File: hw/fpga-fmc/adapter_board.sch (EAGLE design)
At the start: 19 parts, among them J1 5569262-1, J2 ASP-134488-01, U1 LTM2881, U10 LTM2881, U11 LTM2881, U12 LTM2881, U13 LTM2881, U14 LTM2881, U15 LTM2881, U16 LTM2881, U2 LTM2881, U3 LTM2881, U4 LTM2881, U5 LTM2881, U6 LTM2881, U7 LTM2881, U8 LTM2881, U9 LTM2881

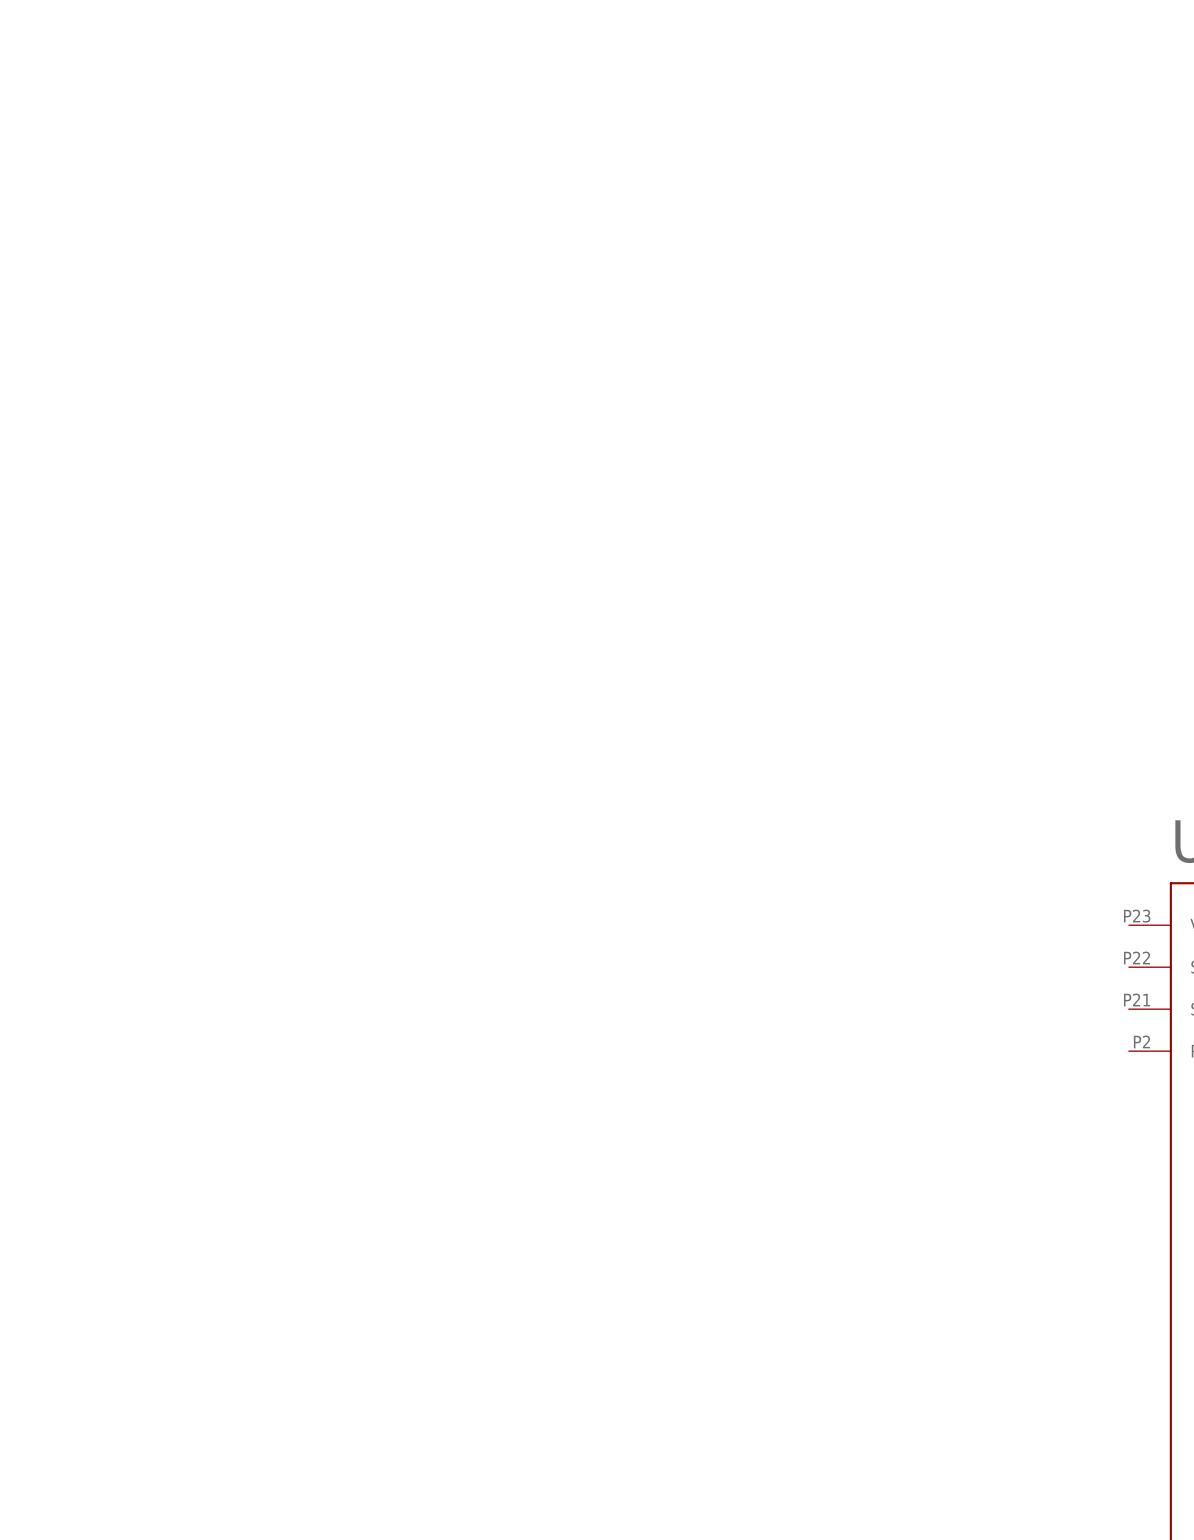
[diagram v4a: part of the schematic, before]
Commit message: fpga-fmc: add 4 channel isolator ic
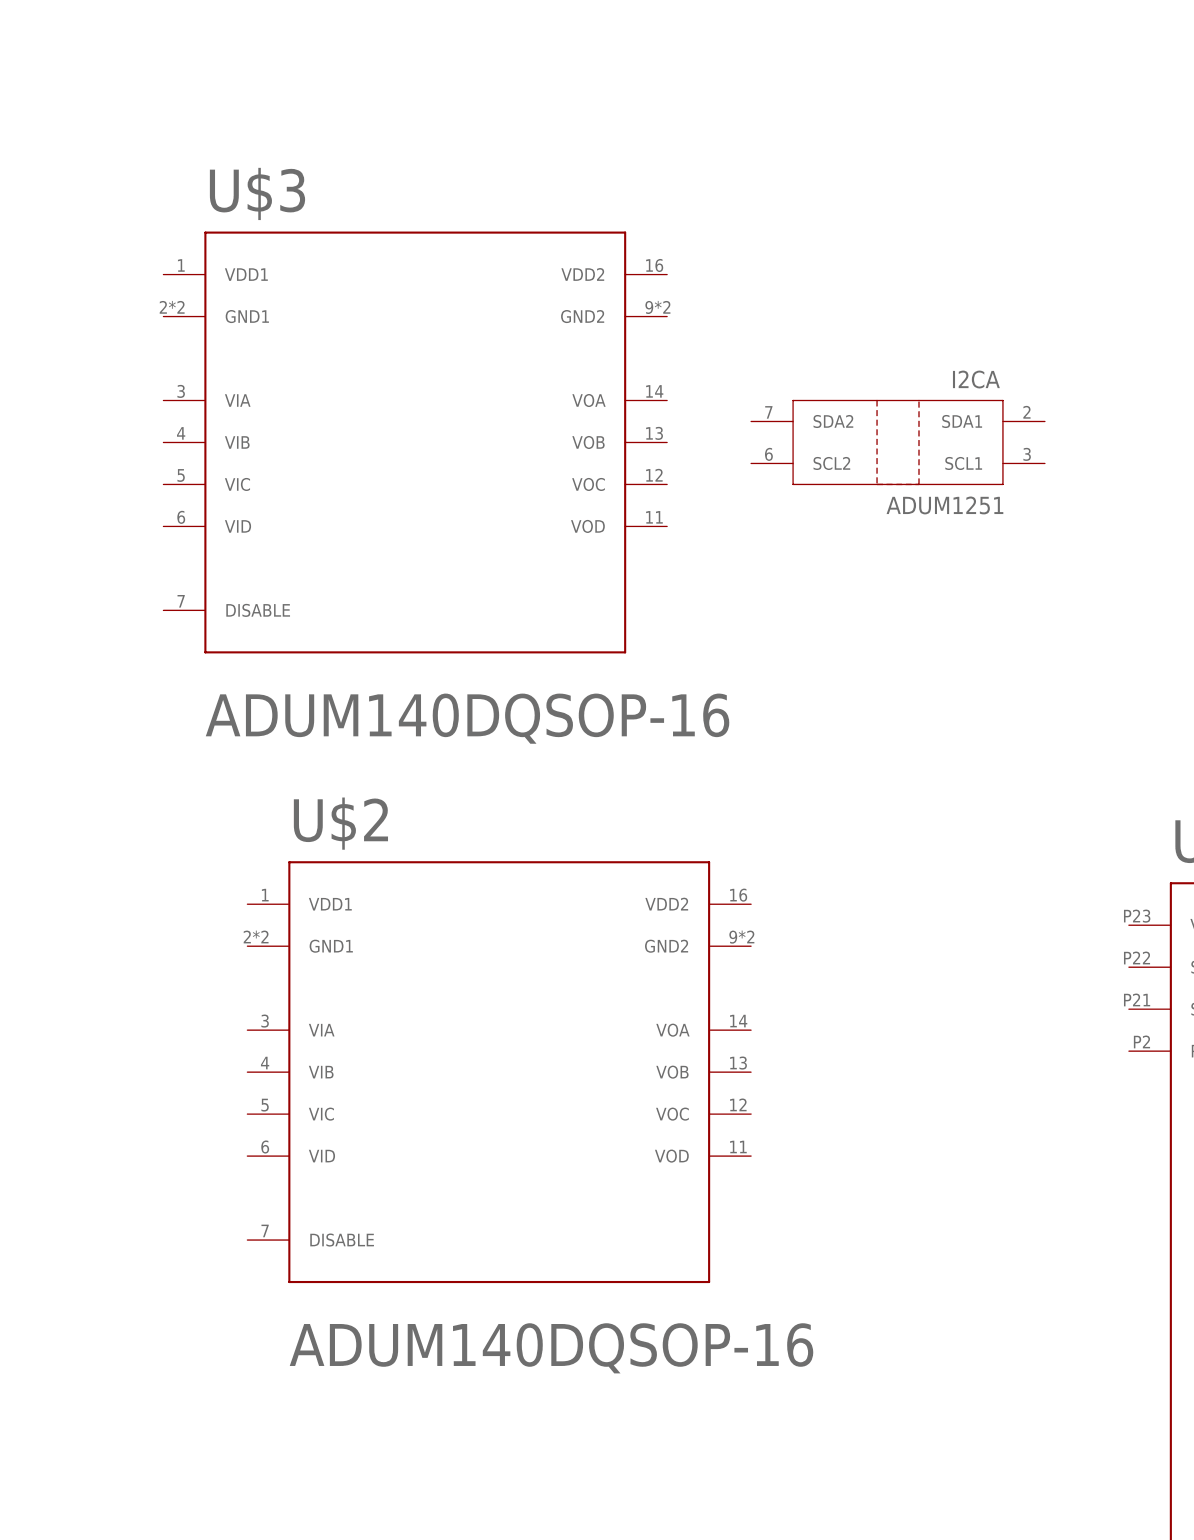
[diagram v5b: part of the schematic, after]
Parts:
- added I2C: ADUM1251, ADUM1251WARZ:ADUM1251WARZ
- added U$2, U$3: ADUM140DQSOP-16, parts:ADUM140DQSOP-16
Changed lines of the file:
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@@
 <part name="U16" library="parts" deviceset="LTM2881" device=""/>
 <part name="U$1" library="parts" deviceset="PCA9548A" device=""/>
+<part name="I2C" library="ADUM1251WARZ" deviceset="ADUM1251WARZ" device="" value="ADUM1251">
+<attribute name="DIGIKEY" value="ADUM1251ARZ-RL7TR-ND"/>
+</part>
+<part name="U$2" library="parts" deviceset="ADUM140D" device="QSOP-16" package3d_urn="urn:adsk.eagle:package:3955/1"/>
+<part name="U$3" library="parts" deviceset="ADUM140D" device="QSOP-16" package3d_urn="urn:adsk.eagle:package:3955/1"/>
 </parts>
 <sheets>
@@
 <attribute name="NAME" x="10.16" y="-10.16" size="5.08" layer="95"/>
 <attribute name="VALUE" x="10.16" y="-129.54" size="5.08" layer="95"/>
+</instance>
+<instance part="I2C" gate="A" x="-22.86" y="40.64" smashed="yes" rot="MR0">
+<attribute name="NAME" x="-10.5156" y="47.2186" size="2.0828" layer="95" ratio="6" rot="SMR0"/>
+<attribute name="VALUE" x="-9.8806" y="31.9786" size="2.0828" layer="96" ratio="6" rot="SMR0"/>
+<attribute name="DIGIKEY" x="-22.86" y="40.64" size="1.778" layer="96" rot="MR0" display="off"/>
+</instance>
+<instance part="U$2" gate="G$1" x="-71.12" y="-35.56" smashed="yes">
+<attribute name="NAME" x="-96.52" y="-7.62" size="5.08" layer="95"/>
+<attribute name="VALUE" x="-96.52" y="-71.12" size="5.08" layer="96"/>
+</instance>
+<instance part="U$3" gate="G$1" x="-81.28" y="40.64" smashed="yes">
+<attribute name="NAME" x="-106.68" y="68.58" size="5.08" layer="95"/>
+<attribute name="VALUE" x="-106.68" y="5.08" size="5.08" layer="96"/>
 </instance>
 </instances>
@@
 will not be understood (or retained) with this version.
 </note>
+<note version="8.3" severity="warning">
+Since Version 8.3, EAGLE supports the association of 3D packages
+with devices in libraries, schematics, and board files. Those 3D
+packages will not be understood (or retained) with this version.
+</note>
 </compatibility>

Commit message: hw/fpga-fmc: add and route rs485 transceiver for 3 channels
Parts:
- removed U10, U11, U12, U13, U14, U15, U16, U7, U8, U9: LTM2881, parts:LTM2881
- added C1, C10, C11, C12, C13, C14, C2, C3, C5, C6, C7, C8, C9: 100n, rcl:C-EUC0805
- added C4: 1u, rcl:C-EUC0805
- added R1, R10, R11, R12, R13, R14, R15, R16, R17, R18, R19, R20, R21, R22, R24, R26, R28, R3, R30, R4, R5, R6, R7, R8, R9: (no value), rcl:R-EU_R0805
- added R2, R23, R25, R27, R29, R31: 100R, rcl:R-EU_R0805
- U1, U2, U3, U4, U5, U6: value LTM2881 -> ADM3066E; device parts:LTM2881 -> parts:ADM3066E
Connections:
- net N$10 renamed RJ6_SDO
- net N$11 renamed RJ6_SCL
- net N$12 renamed RJ6_DATA_P
- net N$13 renamed RJ6_CONV
- net N$15 renamed RJ6_DATA_N
- net N$16 renamed RJ6_CLK_N
- net N$17 renamed RJ6_CLK_P
- net N$2 renamed RJ5_SDO
- net N$26 renamed RJ7_SDO
- net N$27 renamed RJ7_SCL
- net N$29 renamed RJ7_CONV
- net N$3 renamed RJ5_SCL
- net N$34 renamed RJ8_SDO
- net N$35 renamed RJ8_SCL
- net N$37 renamed RJ8_CONV
- net N$4 renamed RJ5_DATA_P
- net N$5 renamed RJ5_CONV
- net N$7 renamed RJ5_DATA_N
- net N$8 renamed RJ5_CLK_N
- net N$9 renamed RJ5_CLK_P
- removed net N$28: J1.7.6
- removed net N$31: J1.7.3
- removed net N$32: J1.7.2
- removed net N$33: J1.7.1
- removed net N$36: J1.8.6
- removed net N$39: J1.8.3
- removed net N$40: J1.8.2
- removed net N$57: J1.8.1
- removed net U1_ON: U1.ON
- new net 3V3: C3.2, C4.2, U$1.VCC
- new net 5V: C10.1, C12.1, C14.1, C2.1, C6.1, C8.1, R10.2, R11.2, R12.2, R13.2, R14.2, R15.2, R16.2, R17.2, R18.2, R19.2, R20.2, R21.2, R3.2, R4.2, R8.2, R9.2, U1.VCC, U2.VCC, U3.VCC, U4.VCC, U5.VCC, U6.VCC
- new net LSIO1: R2.1, U1.DI, U1.RO
- new net LSIO2: R23.1, U2.DI, U2.RO
- new net LSIO3: R25.1, U3.DI, U3.RO
- new net LSIO4: R27.1, U4.DI, U4.RO
- new net LSIO5: R29.1, U5.DI, U5.RO
- new net LSIO6: R31.1, U6.DI, U6.RO
- new net N$1: R3.1, U$1.SD0
- new net N$14: R8.1, U$1.SD1
- new net N$21: U$1.SD3
- new net N$22: R12.1, R13.1, U$1.SC3
- new net N$24: R15.1, U$1.SC4
- new net N$46: R7.1, U$1.RESET
- new net N$6: R4.1, U$1.SC0
- new net RJ7_CLK_N: J1.7.2, R28.2, U5.B
- new net RJ7_CLK_P: J1.7.1, R28.1, U5.A
- new net RJ7_DATA_N: J1.7.3, R30.2, U6.B
- new net RJ7_DATA_P: J1.7.6, R30.1, U6.A
- new net RJ8_CLK_N: J1.8.2, R1.2, U1.B
- new net RJ8_CLK_P: J1.8.1, R1.1, U1.A
- new net RJ8_DATA_N: J1.8.3, R22.2, U2.B
- new net RJ8_DATA_P: J1.8.6, R22.1, U2.A
- net +3V3: no longer U1.VCC1
- net 0V: now also C1.2, C10.2, C11.2, C12.2, C13.2, C14.2, C2.2, C3.1, C4.1, C5.2, C6.2, C7.2, C8.2, C9.2, U$1.A0, U$1.A1, U$1.A2, U$1.GND, U1.GND, U2.GND, U3.GND, U4.GND, U5.GND, U6.GND; no longer U1.GND1
- net 1V8: now also C1.1, C11.1, C13.1, C5.1, C7.1, C9.1, R5.2, R6.2, R7.2, U1.VIO, U2.VIO, U3.VIO, U4.VIO, U5.VIO, U6.VIO; no longer U1.VL
- net FMC_DP0_C2M_N: now also U1.DE, U1.RE
- net FMC_DP0_C2M_P: now also R2.2
- net FMC_DP0_M2C_N: now also R27.2
- net FMC_DP0_M2C_P: now also U4.DE, U4.RE
- net FMC_LA00_CC_N: now also R23.2
- net FMC_LA00_CC_P: now also U2.DE, U2.RE
- net FMC_LA02_N: now also R25.2
- net FMC_LA02_P: now also U3.DE, U3.RE
- net FMC_LA03_N: now also R31.2
- net FMC_LA03_P: now also U6.DE, U6.RE
- net FMC_LA04_N: now also R29.2
- net FMC_LA04_P: now also U5.DE, U5.RE
- net FMC_LA06_N: no longer U1.DI
- net FMC_LA06_P: no longer U1.RO
- net N$18: now also R9.1, U$1.SC1; no longer U1.RE
- net N$19: now also R10.1, U$1.SD2; no longer U1.TE
- net N$20: now also R11.1, U$1.SC2; no longer U1.DE
- net N$23: now also R14.1, U$1.SD4; no longer U1.DOUT
- net N$25: now also R16.1, U$1.SD5; no longer U1.VCC2
- net N$30: now also R17.1, U$1.SC5; no longer U1.A
- net N$38: now also R18.1, U$1.SD6; no longer U1.B
- net N$41: now also R19.1, U$1.SC6; no longer U1.Y
- net N$42: now also R20.1, U$1.SD7; no longer U1.Z
- net N$43: now also R21.1, U$1.SC7; no longer U1.SLO
- net N$44: now also R5.1, U$1.SDA; no longer U1.DIN
- net N$45: now also R6.1, U$1.SCL; no longer U1.GND2
- net RJ4_CLK_N: now also R24.2, U3.B
- net RJ4_CLK_P: now also R24.1, U3.A
- net RJ4_DATA_N: now also R26.2, U4.B
- net RJ4_DATA_P: now also R26.1, U4.A
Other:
- note added: "CLK IO 4"
- note added: "CLK IO 7"
- note added: "CLK IO 8"
- note added: "DATA IO 4"
- note added: "DATA IO 7"
- note added: "DATA IO 8"
- moved on the sheet: U$1

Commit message: fpga-fmc: add i2c circuit and level shifter for conv signal
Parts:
- removed I2C: ADUM1251, ADUM1251WARZ:ADUM1251WARZ
- removed U$3: ADUM140DQSOP-16, parts:ADUM140DQSOP-16
- added C15, C16, C17, C18, C19, C20, C21, C22, C23, C24, C25, C26, C27, C28, C29, C30, C31, C32, C33, C34, C35, C36, C37, C39: 100n, rcl:C-EUC0805
- added IC1: M24C02, parts:N24C02UDTG
- added R32, R34, R36, R38, R40, R42, R44, R46, R48, R50: (no value), rcl:R-EU_R0805
- added R33, R35, R37, R39, R41, R43, R45, R47, R49, R51: 100R, rcl:R-EU_R0805
- added R52: 0R, rcl:R-EU_R0805
- added U10, U11, U12, U13, U14, U15, U16, U7, U8, U9: ADM3066E, parts:ADM3066E
- added U17: TCA9548A, parts:PCA9548A
- J2: SPICEPREFIX (none) -> X
- R10, R11, R12, R13, R14, R15, R16, R17, R18, R19, R20, R21, R3, R4, R5, R6, R8, R9: value (none) -> 1k
- R7: value (none) -> 10k
- U$1: value PCA9548A -> TXS0104E; device parts:PCA9548A -> parts:TXS0104E
- U$2: value ADUM140DQSOP-16 -> TXS0104E; device parts:ADUM140DQSOP-16 -> parts:TXS0104E
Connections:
- removed net 3V3: C3.2, C4.2, U$1.VCC
- removed net N$18: R9.1, U$1.SC1
- removed net N$19: R10.1, U$1.SD2
- removed net N$20: R11.1, U$1.SC2
- removed net N$21: U$1.SD3
- removed net N$22: R12.1, R13.1, U$1.SC3
- removed net N$23: R14.1, U$1.SD4
- removed net N$24: R15.1, U$1.SC4
- removed net N$25: R16.1, U$1.SD5
- removed net N$30: R17.1, U$1.SC5
- removed net N$38: R18.1, U$1.SD6
- removed net N$41: R19.1, U$1.SC6
- removed net N$42: R20.1, U$1.SD7
- removed net N$43: R21.1, U$1.SC7
- new net 3P3VAUX: C39.2, IC1.VCC, J2D.D32, R52.2
- new net GA0: IC1.A1, J2C.C34
- new net GA1: IC1.A0, J2D.D35
- new net LSIO10: R39.1, U10.DI, U10.RO
- new net LSIO11: R41.1, U11.DI, U11.RO
- new net LSIO12: R43.1, U12.DI, U12.RO
- new net LSIO13: R45.1, U13.DI, U13.RO
- new net LSIO14: R47.1, U14.DI, U14.RO
- new net LSIO15: R49.1, U15.DI, U15.RO
- new net LSIO16: R51.1, U16.DI, U16.RO
- new net LSIO7: R33.1, U7.DI, U7.RO
- new net LSIO8: R35.1, U8.DI, U8.RO
- new net LSIO9: R37.1, U9.DI, U9.RO
- new net N$10: U$2.B4
- new net N$11: U$2.B3
- new net N$12: U$2.B2
- new net N$13: U$2.B1
- new net N$15: U$1.B3
- new net N$16: U$1.B2
- new net N$17: U$1.B1
- new net N$2: U$2.A4
- new net N$3: U$2.A3
- new net N$4: U$2.A2
- new net N$5: U$2.A1
- new net N$7: U$1.A3
- new net N$8: U$1.A2
- new net N$9: U$1.A1
- net +12V: now also C37.2
- net +3V3: now also C36.2; no longer J2D.D32
- net 0V: now also C15.2, C16.2, C17.2, C18.2, C19.2, C20.2, C21.2, C22.2, C23.2, C24.2, C25.2, C26.2, C27.2, C28.2, C29.2, C30.2, C31.2, C32.2, C33.2, C34.2, C35.1, C36.1, C37.1, C39.1, IC1.A2, IC1.GND, J2G$1.P$1, U$2.GND, U10.GND, U11.GND, U12.GND, U13.GND, U14.GND, U15.GND, U16.GND, U17.A0, U17.A1, U17.A2, U17.GND, U7.GND, U8.GND, U9.GND; no longer J2C.C34, J2D.D35, U$1.A0, U$1.A1, U$1.A2
- net 1V8: now also C15.1, C17.1, C19.1, C21.1, C23.1, C25.1, C27.1, C29.1, C3.2, C31.1, C33.1, C4.2, U$1.OE, U$1.VCCA, U$2.OE, U$2.VCCA, U10.VIO, U11.VIO, U12.VIO, U13.VIO, U14.VIO, U15.VIO, U16.VIO, U17.VCC, U7.VIO, U8.VIO, U9.VIO
- net 5V: now also C16.1, C18.1, C20.1, C22.1, C24.1, C26.1, C28.1, C30.1, C32.1, C34.1, U$1.VCCB, U$2.VCCB, U10.VCC, U11.VCC, U12.VCC, U13.VCC, U14.VCC, U15.VCC, U16.VCC, U7.VCC, U8.VCC, U9.VCC
- net FMC_DP0_C2M_N: now also U9.DE, U9.RE
- net FMC_DP0_C2M_P: now also R37.2
- net FMC_DP0_M2C_N: now also R43.2
- net FMC_DP0_M2C_P: now also U12.DE, U12.RE
- net FMC_IIC_SCL: now also IC1.SCL
- net FMC_IIC_SDA: now also IC1.SDA
- net FMC_LA00_CC_N: now also R39.2
- net FMC_LA00_CC_P: now also U10.DE, U10.RE
- net FMC_LA01_CC_N: now also R33.2, R49.2
- net FMC_LA01_CC_P: now also U15.DE, U15.RE, U7.DE, U7.RE
- net FMC_LA02_N: now also R41.2
- net FMC_LA02_P: now also U11.DE, U11.RE
- net FMC_LA03_N: now also R35.2, R47.2, R51.2
- net FMC_LA03_P: now also U14.DE, U14.RE, U16.DE, U16.RE, U8.DE, U8.RE
- net FMC_LA04_N: now also R45.2
- net FMC_LA04_P: now also U13.DE, U13.RE
- net N$1: now also IC1.WP, R52.1; no longer R3.1, U$1.SD0
- net N$14: now also U$1.B4; no longer R8.1, U$1.SD1
- net N$44: now also U17.SDA; no longer U$1.SDA
- net N$45: now also U17.SCL; no longer U$1.SCL
- net N$46: now also U17.RESET; no longer U$1.RESET
- net N$6: now also U$1.A4; no longer R4.1, U$1.SC0
- net RJ1_CLK_N: now also R48.2, U15.B
- net RJ1_CLK_P: now also R48.1, U15.A
- net RJ1_DATA_N: now also R50.2, U16.B
- net RJ1_DATA_P: now also R50.1, U16.A
- net RJ1_SCL: now also R17.1, U17.SC5
- net RJ1_SDO: now also R16.1, U17.SD5
- net RJ2_CLK_N: now also R40.2, U11.B
- net RJ2_CLK_P: now also R40.1, U11.A
- net RJ2_DATA_N: now also R42.2, U12.B
- net RJ2_DATA_P: now also R42.1, U12.A
- net RJ2_SCL: now also R21.1, U17.SC7
- net RJ2_SDO: now also R20.1, U17.SD7
- net RJ3_CLK_N: now also R32.2, U7.B
- net RJ3_CLK_P: now also R32.1, U7.A
- net RJ3_DATA_N: now also R34.2, U8.B
- net RJ3_DATA_P: now also R34.1, U8.A
- net RJ3_SCL: now also R9.1, U17.SC1
- net RJ3_SDO: now also R8.1, U17.SD1
- net RJ4_SCL: now also R13.1, U17.SC3
- net RJ4_SDO: now also R12.1, U17.SD3
- net RJ5_CLK_N: now also R44.2, U13.B
- net RJ5_CLK_P: now also R44.1, U13.A
- net RJ5_DATA_N: now also R46.2, U14.B
- net RJ5_DATA_P: now also R46.1, U14.A
- net RJ5_SCL: now also R15.1, U17.SC4
- net RJ5_SDO: now also R14.1, U17.SD4
- net RJ6_CLK_N: now also R36.2, U9.B
- net RJ6_CLK_P: now also R36.1, U9.A
- net RJ6_DATA_N: now also R38.2, U10.B
- net RJ6_DATA_P: now also R38.1, U10.A
- net RJ6_SCL: now also R19.1, U17.SC6
- net RJ6_SDO: now also R18.1, U17.SD6
- net RJ7_SCL: now also R4.1, U17.SC0
- net RJ7_SDO: now also R3.1, U17.SD0
- net RJ8_SCL: now also R11.1, U17.SC2
- net RJ8_SDO: now also R10.1, U17.SD2
- net V+: now also C35.2
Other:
- note added: "According to https://ohwr.org/project/ed/wikis/schematics-checklist#fmc-mezzanine-cards"
- note added: "CLK IO 1"
- note added: "CLK IO 2"
- note added: "CLK IO 3"
- note added: "CLK IO 5"
- note added: "CLK IO 6"
- note added: "DATA IO 1"
- note added: "DATA IO 2"
- note added: "DATA IO 3"
- note added: "DATA IO 5"
- note added: "DATA IO 6"
- note added: "EEPROM required to fulfill VITA Standard. Contains setting for V_ADJ"

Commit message: fpga_fmc: route conv signals and more rj channels
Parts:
- added R54, R55: (no value), rcl:R-EU_R0805
- added U$3: TXS0102, parts:TXS0102
- U$1: value TXS0104E -> TXS0102; device parts:TXS0104E -> parts:TXS0102
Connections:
- net N$46 renamed I2C_RESET
- removed net N$10: U$2.B4
- removed net N$11: U$2.B3
- removed net N$12: U$2.B2
- removed net N$14: U$1.B4
- removed net N$15: U$1.B3
- removed net N$16: U$1.B2
- removed net N$17: U$1.B1
- removed net N$44: R5.1, U17.SDA
- removed net N$45: R6.1, U17.SCL
- removed net N$6: U$1.A4
- removed net N$7: U$1.A3
- removed net N$8: U$1.A2
- removed net N$9: U$1.A1
- new net CONV_OE: R55.2, U$1.OE, U$3.OE
- net 0V: now also R54.1, R55.1, U$3.GND
- net 1V8: now also U$3.VCCA; no longer U$1.OE, U$2.OE
- net 5V: now also U$3.VCCB
- net FMC_DP0_C2M_N: no longer U9.DE, U9.RE
- net FMC_DP0_C2M_P: no longer R37.2
- net FMC_DP0_M2C_N: no longer R43.2
- net FMC_DP0_M2C_P: no longer U12.DE, U12.RE
- net FMC_LA00_CC_N: no longer R39.2
- net FMC_LA00_CC_P: no longer U10.DE, U10.RE
- net FMC_LA01_CC_N: now also R31.2; no longer R33.2, R49.2
- net FMC_LA01_CC_P: now also U6.DE, U6.RE; no longer U15.DE, U15.RE, U7.DE, U7.RE
- net FMC_LA02_N: no longer R41.2
- net FMC_LA02_P: no longer U11.DE, U11.RE
- net FMC_LA03_N: now also R29.2; no longer R31.2, R35.2, R47.2, R51.2
- net FMC_LA03_P: now also U5.DE, U5.RE; no longer U14.DE, U14.RE, U16.DE, U16.RE, U6.DE, U6.RE, U8.DE, U8.RE
- net FMC_LA04_N: now also U$1.A1; no longer R29.2, R45.2
- net FMC_LA04_P: now also U$1.A2; no longer U13.DE, U13.RE, U5.DE, U5.RE
- net FMC_LA05_N: now also R35.2
- net FMC_LA05_P: now also U8.DE, U8.RE
- net FMC_LA06_N: now also R33.2
- net FMC_LA06_P: now also U7.DE, U7.RE
- net FMC_LA07_N: now also R39.2
- net FMC_LA07_P: now also U10.DE, U10.RE
- net FMC_LA08_N: now also U$3.A1
- net FMC_LA08_P: now also U$3.A2
- net FMC_LA09_N: now also R37.2
- net FMC_LA09_P: now also U9.DE, U9.RE
- net FMC_LA10_N: now also R6.1, U17.SCL
- net FMC_LA10_P: now also R5.1, U17.SDA
- net FMC_LA11_N: now also R51.2
- net FMC_LA11_P: now also U16.DE, U16.RE
- net FMC_LA12_N: now also R45.2
- net FMC_LA12_P: now also U13.DE, U13.RE
- net FMC_LA13_N: now also R43.2
- net FMC_LA13_P: now also U12.DE, U12.RE
- net FMC_LA14_N: now also R41.2
- net FMC_LA14_P: now also U11.DE, U11.RE
- net FMC_LA15_N: now also R49.2
- net FMC_LA15_P: now also U15.DE, U15.RE
- net FMC_LA16_N: now also R47.2
- net FMC_LA16_P: now also U14.DE, U14.RE
- net N$13: now also R54.2, U$2.OE; no longer U$2.B1
- net RJ1_CONV: now also U$2.B4
- net RJ2_CONV: now also U$2.B1
- net RJ3_CONV: now also U$3.B2
- net RJ4_CONV: now also U$1.B2
- net RJ5_CONV: now also U$2.B3
- net RJ6_CONV: now also U$2.B2
- net RJ7_CONV: now also U$3.B1
- net RJ8_CONV: now also U$1.B1
